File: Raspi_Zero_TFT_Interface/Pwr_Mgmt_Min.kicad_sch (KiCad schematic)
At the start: 18 parts, among them Q4 SSM3J358R, SW2 Rocker Switch SPST, U11 MCP73831-2-OT, U13 LD39050

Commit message: First draft layout of power pi board
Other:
- sheet OverVoltageProtection1: file OVP_Circuit.kicad_sch -> C:/Users/cdeli/Desktop/DataCore/TraumaChek/GenII/SchematicAndBoardFiles/Power_Management_Board/OVP_Circuit.kicad_sch
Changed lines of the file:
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@@
 	(text "For longevity of battery, we\nmay want to limit peak voltage \nof the battery. "
 		(exclude_from_sim no)
-		(at 27.686 30.988 0)
+		(at 80.264 26.67 0)
 		(effects
 			(font
@@
 			)
 		)
-		(property "Sheetfile" "OVP_Circuit.kicad_sch"
+		(property "Sheetfile" "C:/Users/cdeli/Desktop/DataCore/TraumaChek/GenII/SchematicAndBoardFiles/Power_Management_Board/OVP_Circuit.kicad_sch"
 			(at 74.93 102.1846 0)
 			(effects
@@
 				)
 				(justify left top)
-			)
-		)
+				(hide yes)
+			)
+		)

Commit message: Completed (unflipped) board
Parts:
- added R3: 10k, Resistor_SMD:R_0603_1608Metric_Pad0.98x0.95mm_HandSolder, symbol Device:R_Small_US
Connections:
- net GND: now also R3.2
- net V_Input: now also D8.1 (K), Q4.2 (S), SW2.1 (A), R3.1; no longer SW2.2 (B), U13.1 (EN)
- new net: SW2.2 (B), U13.1 (EN)
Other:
- note added: "Use Cases: 1) Switch Off, charger plugged in: G = 0->5V, S = 0->4.3V, P-FET Off 2) Charger stays In, Switch flipped ON: G = 5V, S = 4.3V, P-FET Off 3) Charger Removed, switch stays on: G = 5->0V, S = 4.3, P-FET turns on, S->3.7V 4) Switch Turned Off, charger stays removed: G = 0V, S = 3.7->0V, P-FET turns off after a few time constants."
- note removed: "USB_VCC 1 and 2 should be monitored by MCU ADC channels to determine how much current source can supply. If too low, MCU should not allow certain functions and warn the user."
- moved on the sheet: SW2
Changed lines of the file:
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@@
+	)
+	(junction
+		(at 139.7 95.25)
+		(diameter 0)
+		(color 0 0 0 0)
 	)
 	(junction
@@
 	)
 	(junction
+		(at 143.51 48.26)
+		(diameter 0)
+		(color 0 0 0 0)
+	)
+	(junction
+		(at 144.78 83.82)
+		(diameter 0)
+		(color 0 0 0 0)
+	)
+	(junction
 		(at 185.42 45.72)
 		(diameter 0)
@@
 	)
 	(junction
-		(at 151.13 48.26)
-		(diameter 0)
-		(color 0 0 0 0)
-	)
-	(junction
 		(at 185.42 68.58)
 		(diameter 0)
@@
 	(wire
 		(pts
-			(xy 139.7 48.26) (xy 151.13 48.26)
+			(xy 139.7 48.26) (xy 143.51 48.26)
 		)
 		(stroke
@@
 	(wire
 		(pts
+			(xy 144.78 83.82) (xy 144.78 87.63)
+		)
+		(stroke
+			(width 0)
+			(type default)
+		)
+	)
+	(wire
+		(pts
 			(xy 123.19 74.93) (xy 123.19 83.82)
 		)
@@
 	(wire
 		(pts
+			(xy 139.7 95.25) (xy 144.78 95.25)
+		)
+		(stroke
+			(width 0)
+			(type default)
+		)
+	)
+	(wire
+		(pts
 			(xy 90.17 74.93) (xy 96.52 74.93)
 		)
@@
 	(wire
 		(pts
+			(xy 144.78 53.34) (xy 143.51 53.34)
+		)
+		(stroke
+			(width 0)
+			(type default)
+		)
+	)
+	(wire
+		(pts
 			(xy 185.42 48.26) (xy 185.42 53.34)
 		)
@@
 	(wire
 		(pts
-			(xy 139.7 83.82) (xy 143.51 83.82)
+			(xy 139.7 83.82) (xy 144.78 83.82)
 		)
 		(stroke
@@
 	(wire
 		(pts
-			(xy 151.13 48.26) (xy 185.42 48.26)
-		)
-		(stroke
-			(width 0)
-			(type default)
-		)
-	)
-	(wire
-		(pts
-			(xy 123.19 83.82) (xy 125.73 83.82)
+			(xy 123.19 83.82) (xy 139.7 83.82)
 		)
 		(stroke
@@
 	(wire
 		(pts
+			(xy 139.7 95.25) (xy 139.7 96.52)
+		)
+		(stroke
+			(width 0)
+			(type default)
+		)
+	)
+	(wire
+		(pts
 			(xy 139.7 83.82) (xy 139.7 87.63)
 		)
@@
 	(wire
 		(pts
-			(xy 139.7 92.71) (xy 139.7 96.52)
+			(xy 139.7 92.71) (xy 139.7 95.25)
 		)
 		(stroke
@@
 	(wire
 		(pts
-			(xy 139.7 83.82) (xy 135.89 83.82)
-		)
-		(stroke
-			(width 0)
-			(type default)
-		)
-	)
-	(wire
-		(pts
 			(xy 189.23 36.83) (xy 189.23 39.37)
 		)
@@
 	(wire
 		(pts
+			(xy 144.78 83.82) (xy 147.32 83.82)
+		)
+		(stroke
+			(width 0)
+			(type default)
+		)
+	)
+	(wire
+		(pts
 			(xy 154.94 55.88) (xy 156.21 55.88)
 		)
@@
 	(wire
 		(pts
-			(xy 156.21 53.34) (xy 151.13 53.34)
+			(xy 156.21 53.34) (xy 154.94 53.34)
 		)
 		(stroke
@@
 	(wire
 		(pts
-			(xy 151.13 53.34) (xy 151.13 48.26)
+			(xy 143.51 53.34) (xy 143.51 48.26)
 		)
 		(stroke
@@
 	(wire
 		(pts
+			(xy 143.51 48.26) (xy 185.42 48.26)
+		)
+		(stroke
+			(width 0)
+			(type default)
+		)
+	)
+	(wire
+		(pts
 			(xy 181.61 36.83) (xy 185.42 36.83)
 		)
@@
 	(wire
 		(pts
+			(xy 144.78 92.71) (xy 144.78 95.25)
+		)
+		(stroke
+			(width 0)
+			(type default)
+		)
+	)
+	(wire
+		(pts
 			(xy 91.44 82.55) (xy 96.52 82.55)
 		)
@@
 	(text "Main Power Switch"
 		(exclude_from_sim no)
-		(at 122.428 80.264 0)
+		(at 138.43 43.942 0)
 		(effects
 			(font
@@
 		)
 	)
-	(text "Same LDO used on Nucleo Board"
-		(exclude_from_sim no)
-		(at 138.684 40.386 0)
+	(text "Use Cases:\n1) Switch Off, charger plugged in: G = 0->5V, S = 0->4.3V, P-FET Off\n2) Charger stays In, Switch flipped ON: G = 5V, S = 4.3V, P-FET Off\n3) Charger Removed, switch stays on: G = 5->0V, S = 4.3, P-FET turns on, S->3.7V\n4) Switch Turned Off, charger stays removed: G = 0V, S = 3.7->0V, \nP-FET turns off after a few time constants.  \n"
+		(exclude_from_sim no)
+		(at 15.24 64.516 0)
 		(effects
 			(font
 				(size 1.27 1.27)
 			)
-			(justify left bottom)
-		)
-	)
-	(text "USB_VCC 1 and 2 should be monitored by MCU \nADC channels to determine how much current \nsource can supply. If too low, MCU should not\nallow certain functions and warn the user. "
-		(exclude_from_sim no)
-		(at 46.99 133.35 0)
+			(justify left)
+		)
+	)
+	(text "Same LDO used on Nucleo Board"
+		(exclude_from_sim no)
+		(at 138.684 40.386 0)
 		(effects
 			(font
@@
 	(hierarchical_label "V_Input"
 		(shape output)
-		(at 143.51 83.82 0)
+		(at 147.32 83.82 0)
 		(fields_autoplaced yes)
 		(effects
@@
 	)
 	(symbol
+		(lib_id "Device:R_Small_US")
+		(at 144.78 90.17 0)
+		(unit 1)
+		(exclude_from_sim no)
+		(in_bom yes)
+		(on_board yes)
+		(dnp no)
+		(property "Reference" "R3"
+			(at 149.86 90.17 90)
+			(effects
+				(font
+					(size 1.27 1.27)
+				)
+			)
+		)
+		(property "Value" "10k"
+			(at 147.32 90.17 90)
+			(effects
+				(font
+					(size 1.27 1.27)
+				)
+			)
+		)
+		(property "Footprint" "Resistor_SMD:R_0603_1608Metric_Pad0.98x0.95mm_HandSolder"
+			(at 144.78 90.17 0)
+			(effects
+				(font
+					(size 1.27 1.27)
+				)
+				(hide yes)
+			)
+		)
+		(property "Datasheet" "~"
+			(at 144.78 90.17 0)
+			(effects
+				(font
+					(size 1.27 1.27)
+				)
+				(hide yes)
+			)
+		)
+		(property "Description" ""
+			(at 144.78 90.17 0)
+			(effects
+				(font
+					(size 1.27 1.27)
+				)
+				(hide yes)
+			)
+		)
+		(pin "1"
+		)
+		(pin "2"
+		)
+		(instances
+			(project "Raspi_Zero_TFT_Interface"
+				(path "/9fcf58ec-9ad6-40d8-a93b-d0fc15c15838/50d4a57d-354f-4afa-869e-4e71aa380902"
+					(reference "R3")
+					(unit 1)
+				)
+			)
+		)
+	)
+	(symbol
 		(lib_id "Battery_Management:MCP73831-2-OT")
 		(at 91.44 43.18 0)
@@
 	(symbol
 		(lib_id "Switch:SW_SPST")
-		(at 130.81 83.82 0)
+		(at 149.86 53.34 0)
 		(unit 1)
 		(exclude_from_sim no)
@@
 		(dnp no)
 		(property "Reference" "SW2"
-			(at 130.81 87.884 0)
+			(at 150.368 46.228 0)
 			(effects
 				(font
@@
 		)
 		(property "Value" "Rocker Switch SPST"
-			(at 130.81 80.01 0)
+			(at 149.86 49.53 0)
 			(effects
 				(font
@@
 		)
 		(property "Footprint" "Connector_PinHeader_2.54mm:PinHeader_1x02_P2.54mm_Vertical"
-			(at 130.81 83.82 0)
+			(at 149.86 53.34 0)
 			(effects
 				(font
@@
 		)
 		(property "Datasheet" "~"
-			(at 130.81 83.82 0)
+			(at 149.86 53.34 0)
 			(effects
 				(font
@@
 		)
 		(property "Description" ""
-			(at 130.81 83.82 0)
-			(effects
-				(font
+			(at 149.86 53.34 0)
+			(effects
+				(font

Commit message: Small change to Raspi Board
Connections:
- net V_Input: now also U13.1 (EN); no longer C21.1, D8.1 (K), Q4.2 (S), R3.1
- net at SW2.2 (B): now also C21.1, D8.1 (K), Q4.2 (S), R3.1; no longer U13.1 (EN)
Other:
- moved on the sheet: SW2
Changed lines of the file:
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@@
-	)
-	(junction
-		(at 144.78 83.82)
-		(diameter 0)
-		(color 0 0 0 0)
 	)
 	(junction
@@
 	(wire
 		(pts
+			(xy 139.7 77.47) (xy 139.7 83.82)
+		)
+		(stroke
+			(width 0)
+			(type default)
+		)
+	)
+	(wire
+		(pts
 			(xy 102.87 40.64) (xy 102.87 74.93)
 		)
@@
 	(wire
 		(pts
-			(xy 139.7 48.26) (xy 139.7 83.82)
+			(xy 139.7 48.26) (xy 139.7 67.31)
 		)
 		(stroke
@@
 	(wire
 		(pts
-			(xy 144.78 53.34) (xy 143.51 53.34)
+			(xy 143.51 53.34) (xy 156.21 53.34)
 		)
 		(stroke
@@
 	(wire
 		(pts
+			(xy 143.51 44.45) (xy 143.51 48.26)
+		)
+		(stroke
+			(width 0)
+			(type default)
+		)
+	)
+	(wire
+		(pts
 			(xy 123.19 93.98) (xy 120.65 93.98)
 		)
@@
 	(wire
 		(pts
-			(xy 144.78 83.82) (xy 147.32 83.82)
-		)
-		(stroke
-			(width 0)
-			(type default)
-		)
-	)
-	(wire
-		(pts
 			(xy 154.94 55.88) (xy 156.21 55.88)
 		)
@@
 	(wire
 		(pts
-			(xy 156.21 53.34) (xy 154.94 53.34)
-		)
-		(stroke
-			(width 0)
-			(type default)
-		)
-	)
-	(wire
-		(pts
 			(xy 74.93 34.29) (xy 74.93 35.56)
 		)
@@
 	(wire
 		(pts
+			(xy 146.05 44.45) (xy 143.51 44.45)
+		)
+		(stroke
+			(width 0)
+			(type default)
+		)
+	)
+	(wire
+		(pts
 			(xy 144.78 92.71) (xy 144.78 95.25)
 		)
@@
 	(text "Main Power Switch"
 		(exclude_from_sim no)
-		(at 138.43 43.942 0)
+		(at 119.126 72.39 0)
 		(effects
 			(font
@@
 	(hierarchical_label "V_Input"
 		(shape output)
-		(at 147.32 83.82 0)
+		(at 146.05 44.45 0)
 		(fields_autoplaced yes)
 		(effects
@@
 	(symbol
 		(lib_id "Switch:SW_SPST")
-		(at 149.86 53.34 0)
+		(at 139.7 72.39 270)
 		(unit 1)
 		(exclude_from_sim no)
@@
 		(dnp no)
 		(property "Reference" "SW2"
-			(at 150.368 46.228 0)
+			(at 146.812 72.898 0)
 			(effects
 				(font
@@
 		)
 		(property "Value" "Rocker Switch SPST"
-			(at 149.86 49.53 0)
+			(at 143.51 72.39 0)
 			(effects
 				(font
@@
 		)
 		(property "Footprint" "Connector_PinHeader_2.54mm:PinHeader_1x02_P2.54mm_Vertical"
-			(at 149.86 53.34 0)
+			(at 139.7 72.39 0)
 			(effects
 				(font
@@
 		)
 		(property "Datasheet" "~"
-			(at 149.86 53.34 0)
+			(at 139.7 72.39 0)
 			(effects
 				(font
@@
 		)
 		(property "Description" ""
-			(at 149.86 53.34 0)
-			(effects
-				(font
+			(at 139.7 72.39 0)
+			(effects
+				(font

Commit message: Nearly Finalized Boards
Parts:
- removed C21: 10u, Capacitor_SMD:C_0603_1608Metric_Pad1.08x0.95mm_HandSolder, symbol Device:C_Small
- removed R3: 10k, Resistor_SMD:R_0603_1608Metric_Pad0.98x0.95mm_HandSolder, symbol Device:R_Small_US
- removed U13: LD39050, Package_DFN_QFN:DFN-6-1EP_3x3mm_P0.95mm_EP1.7x2.6mm, symbol FrontEndPrototype_Rev1-rescue:LD39050
- added C4: 22u, Capacitor_SMD:C_0603_1608Metric_Pad1.08x0.95mm_HandSolder, symbol Device:C_Small
- added Q1: SI2347DS-TI-GE3CT, Package_TO_SOT_SMD:SOT-23-3, symbol FrontEndPrototype_Rev1-rescue:SSM3J358R
- added RPU1: 5k, Resistor_SMD:R_0603_1608Metric_Pad0.98x0.95mm_HandSolder, symbol Device:R_Small_US
- added U2: LD39200, Package_DFN_QFN:DFN-6-1EP_3x3mm_P0.95mm_EP1.7x2.6mm, symbol FrontEndPrototype_Rev1-rescue:LD39200_Fixed
- D8: value MSS1P3L -> PMEG3030EP,115; footprint Diode_SMD:D_MicroSMP_AK -> Diode_SMD:D_SOD-128; symbol Device:D -> Device:D_Schottky
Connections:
- net 3V3_Main: now also U2.1 (Vout), U2.2 (ADJ/SENSE)
- net 5V_USB: now also Q1.2 (S); no longer C19.2, D7.2 (A), U11.4 (V_{DD})
- net GND: now also C4.2, RPU1.2, U2.3 (GND)
- net V_Batt+: now also Q4.2 (S); no longer Q4.3 (D)
- net V_Input: now also C4.1, U2.5 (EN), U2.6 (Vin)
- net at D8.1 (K), SW2.2 (B): now also Q4.3 (D); no longer Q4.2 (S)
- net at R20.1: now also U2.4 (PWRGD)
- new net: C19.2, D7.2 (A), Q1.3 (D), U11.4 (V_{DD})
- new net ~{CHARGE_EN}: Q1.1 (G), RPU1.1
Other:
- note added: "- Rds_On should be very low to avoid excess power drain from battery - Continuous drain current must go up to 1A - Can be the same as Charge enable transistor to reduce BOM, but will have higher Ron"
- note added: "Probably Not needed"
- note removed: "- Rds_On should be very low to avoid excess power drain from battery - Continuous drain current must go up to 1A"
- note removed: "Use Cases: 1) Switch Off, charger plugged in: G = 0->5V, S = 0->4.3V, P-FET Off 2) Charger stays In, Switch flipped ON: G = 5V, S = 4.3V, P-FET Off 3) Charger Removed, switch stays on: G = 5->0V, S = 4.3, P-FET turns on, S->3.7V 4) Switch Turned Off, charger stays removed: G = 0V, S = 3.7->0V, P-FET turns off after a few time constants."
- moved on the sheet: C23, C24, C25, C26, D10, Q4, R20

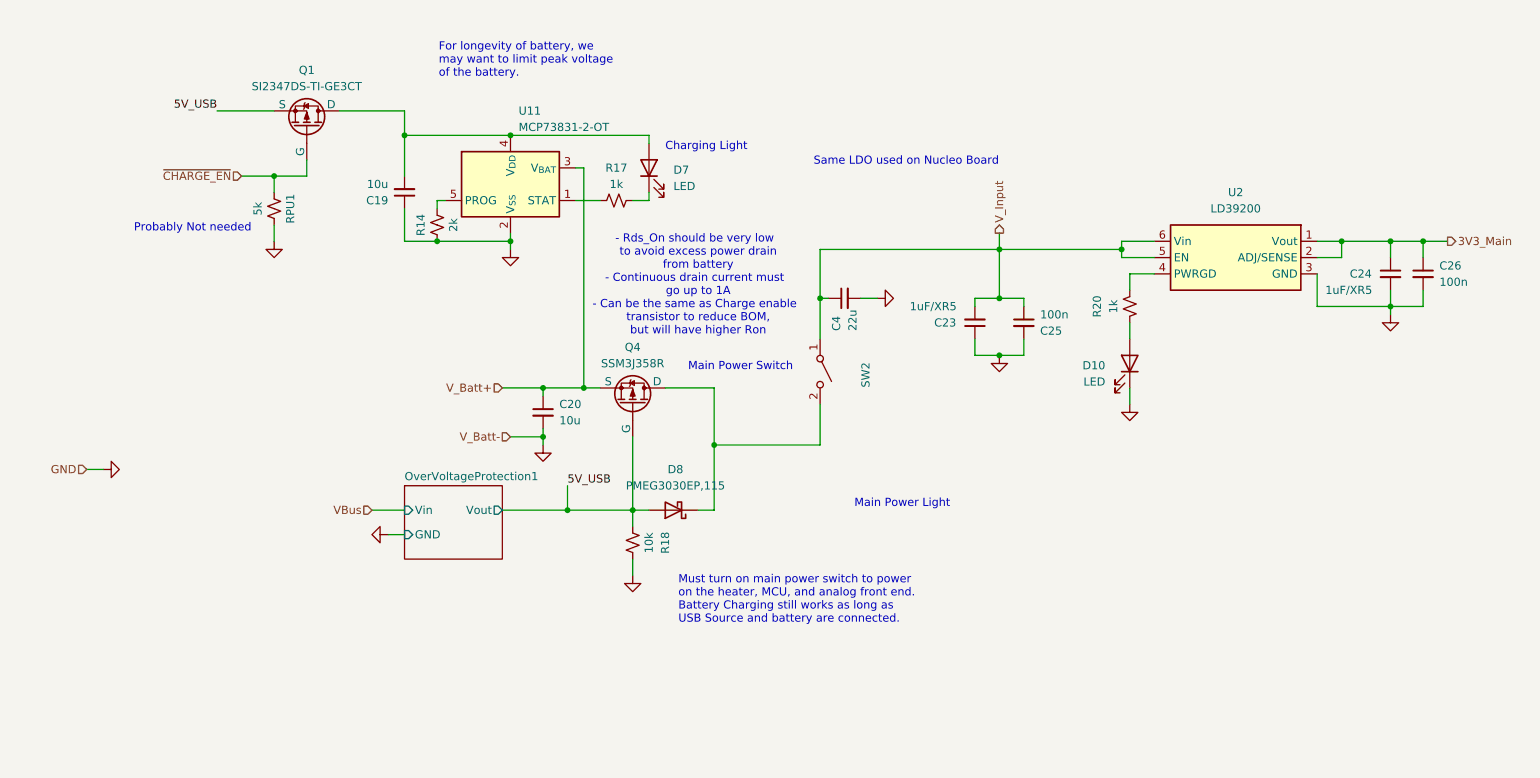
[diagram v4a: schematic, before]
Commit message: First Pass Schematic Fixes for Power Management Board
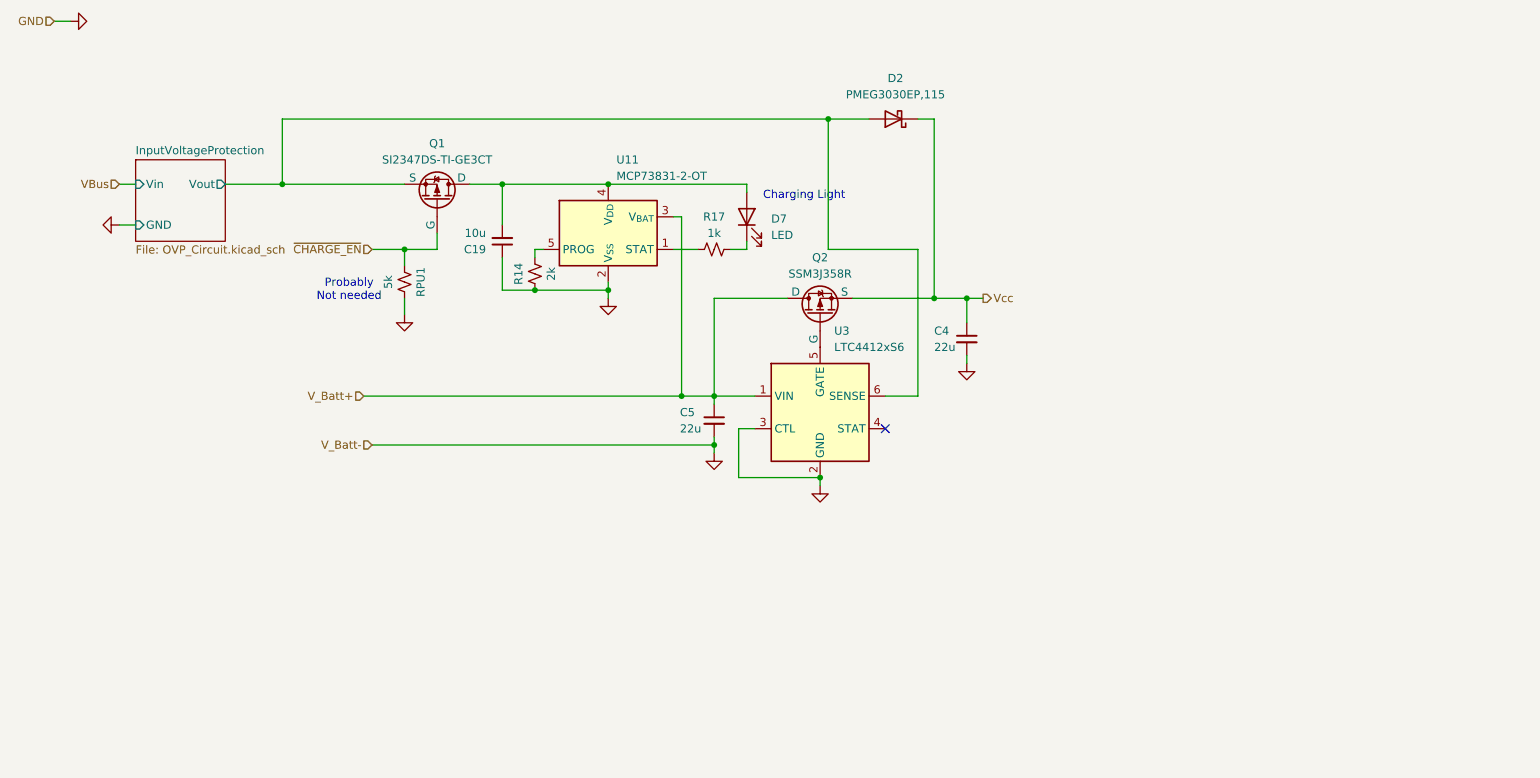
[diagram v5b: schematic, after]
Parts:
- removed C20: 10u, Capacitor_SMD:C_0603_1608Metric_Pad1.08x0.95mm_HandSolder, symbol Device:C_Small
- removed C23, C24: 1uF/XR5, Capacitor_SMD:C_0603_1608Metric_Pad1.08x0.95mm_HandSolder, symbol Device:C_Small
- removed C25, C26: 100n, Capacitor_SMD:C_0603_1608Metric_Pad1.08x0.95mm_HandSolder, symbol Device:C_Small
- removed D10: LED, Diode_THT:D_T-1_P2.54mm_Vertical_AnodeUp, symbol Device:LED
- removed D8: PMEG3030EP,115, Diode_SMD:D_SOD-128, symbol Device:D_Schottky
- removed Q4: SSM3J358R, Package_TO_SOT_SMD:SOT-23-3, symbol FrontEndPrototype_Rev1-rescue:SSM3J358R
- removed R18: 10k, Resistor_SMD:R_0603_1608Metric_Pad0.98x0.95mm_HandSolder, symbol Device:R_Small_US
- removed R20: 1k, Resistor_SMD:R_0603_1608Metric_Pad0.98x0.95mm_HandSolder, symbol Device:R_Small_US
- removed SW2: Rocker Switch SPST, Connector_PinHeader_2.54mm:PinHeader_1x02_P2.54mm_Vertical, symbol Switch:SW_SPST
- removed U2: LD39200, Package_DFN_QFN:DFN-6-1EP_3x3mm_P0.95mm_EP1.7x2.6mm, symbol FrontEndPrototype_Rev1-rescue:LD39200_Fixed
- added C5: 22u, Capacitor_SMD:C_0603_1608Metric_Pad1.08x0.95mm_HandSolder, symbol Device:C_Small
- added D2: PMEG3030EP,115, Diode_SMD:D_SOD-128, symbol Device:D_Schottky
- added Q2: SSM3J358R, Package_TO_SOT_SMD:SOT-23-3, symbol FrontEndPrototype_Rev1-rescue:SSM3J358R
- added U3: LTC4412xS6, Package_TO_SOT_SMD:TSOT-23-6, symbol Power_Management:LTC4412xS6
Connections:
- net GND: now also C5.2, U3.2 (GND), U3.3 (CTL)
- net V_Batt+: now also C5.1, Q2.3 (D), U3.1 (VIN)
- net 5V_USB renamed InputVoltageProtection/Vout
- net InputVoltageProtection/Vout: now also D2.2 (A), U3.6 (SENSE)
- net V_Input renamed Vcc
- net Vcc: now also D2.1 (K), Q2.2 (S)
- new net: Q2.1 (G), U3.5 (GATE)
- no-connect marks 0 -> 1
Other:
- removed sheet OverVoltageProtection1
- added sheet InputVoltageProtection (OVP_Circuit.kicad_sch)
- note removed: "- Rds_On should be very low to avoid excess power drain from battery - Continuous drain current must go up to 1A - Can be the same as Charge enable transistor to reduce BOM, but will have higher Ron"
- note removed: "For longevity of battery, we may want to limit peak voltage of the battery."
- note removed: "Main Power Light"
- note removed: "Main Power Switch"
- note removed: "Must turn on main power switch to power on the heater, MCU, and analog front end. Battery Charging still works as long as USB Source and battery are connected."
- note removed: "Same LDO used on Nucleo Board"
- moved on the sheet: C19, D7, Q1, R14, R17, RPU1, U11
